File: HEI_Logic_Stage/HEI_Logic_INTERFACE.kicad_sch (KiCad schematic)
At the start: 99 parts, among them J1 Conn_02x07_Odd_Even, J2 Conn_02x07_Odd_Even, J4 430450813_Molex, U1 CD40109BQNSRQ1, U16 TLV9051IDBVR, U3 TLV9051IDBVR, U4 TLV9051IDBVR, U7 TLV9051IDBVR, U8 TLV9051IDBVR

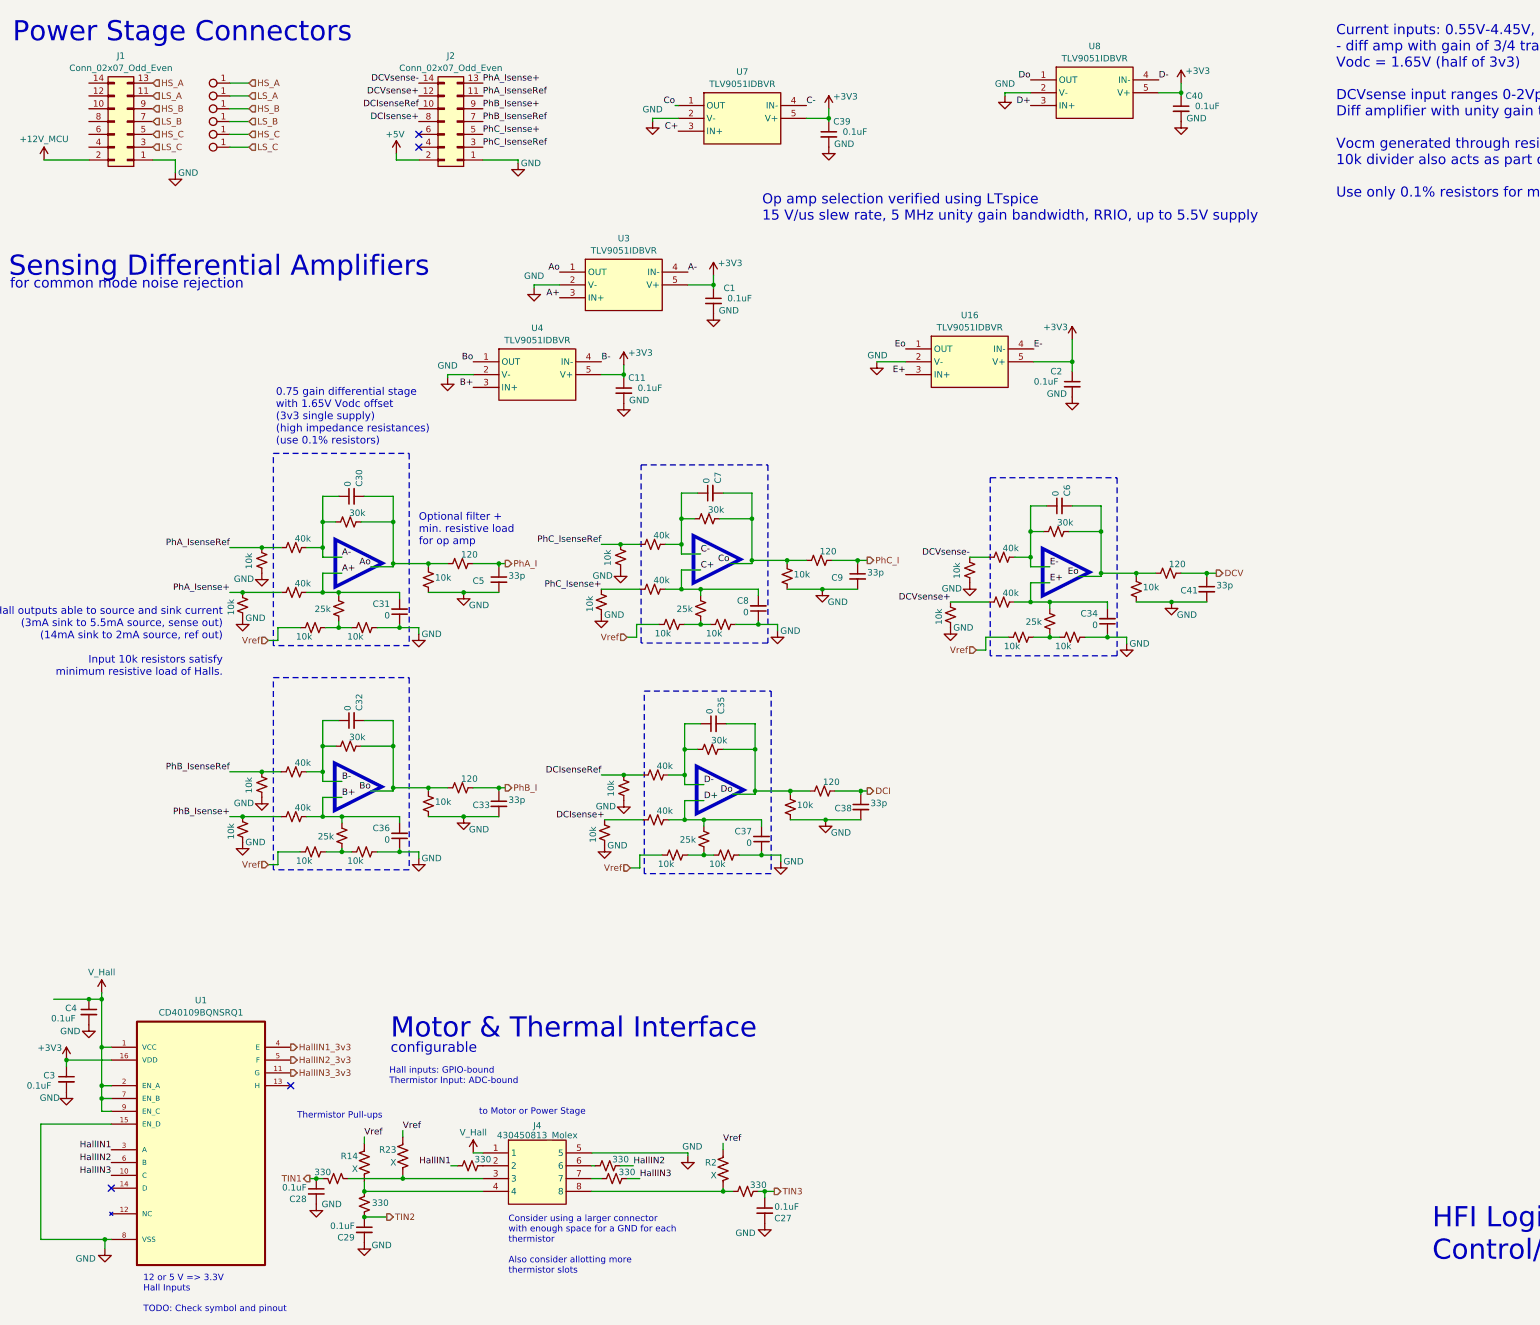
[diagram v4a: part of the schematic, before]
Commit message: almost completed new logic layout
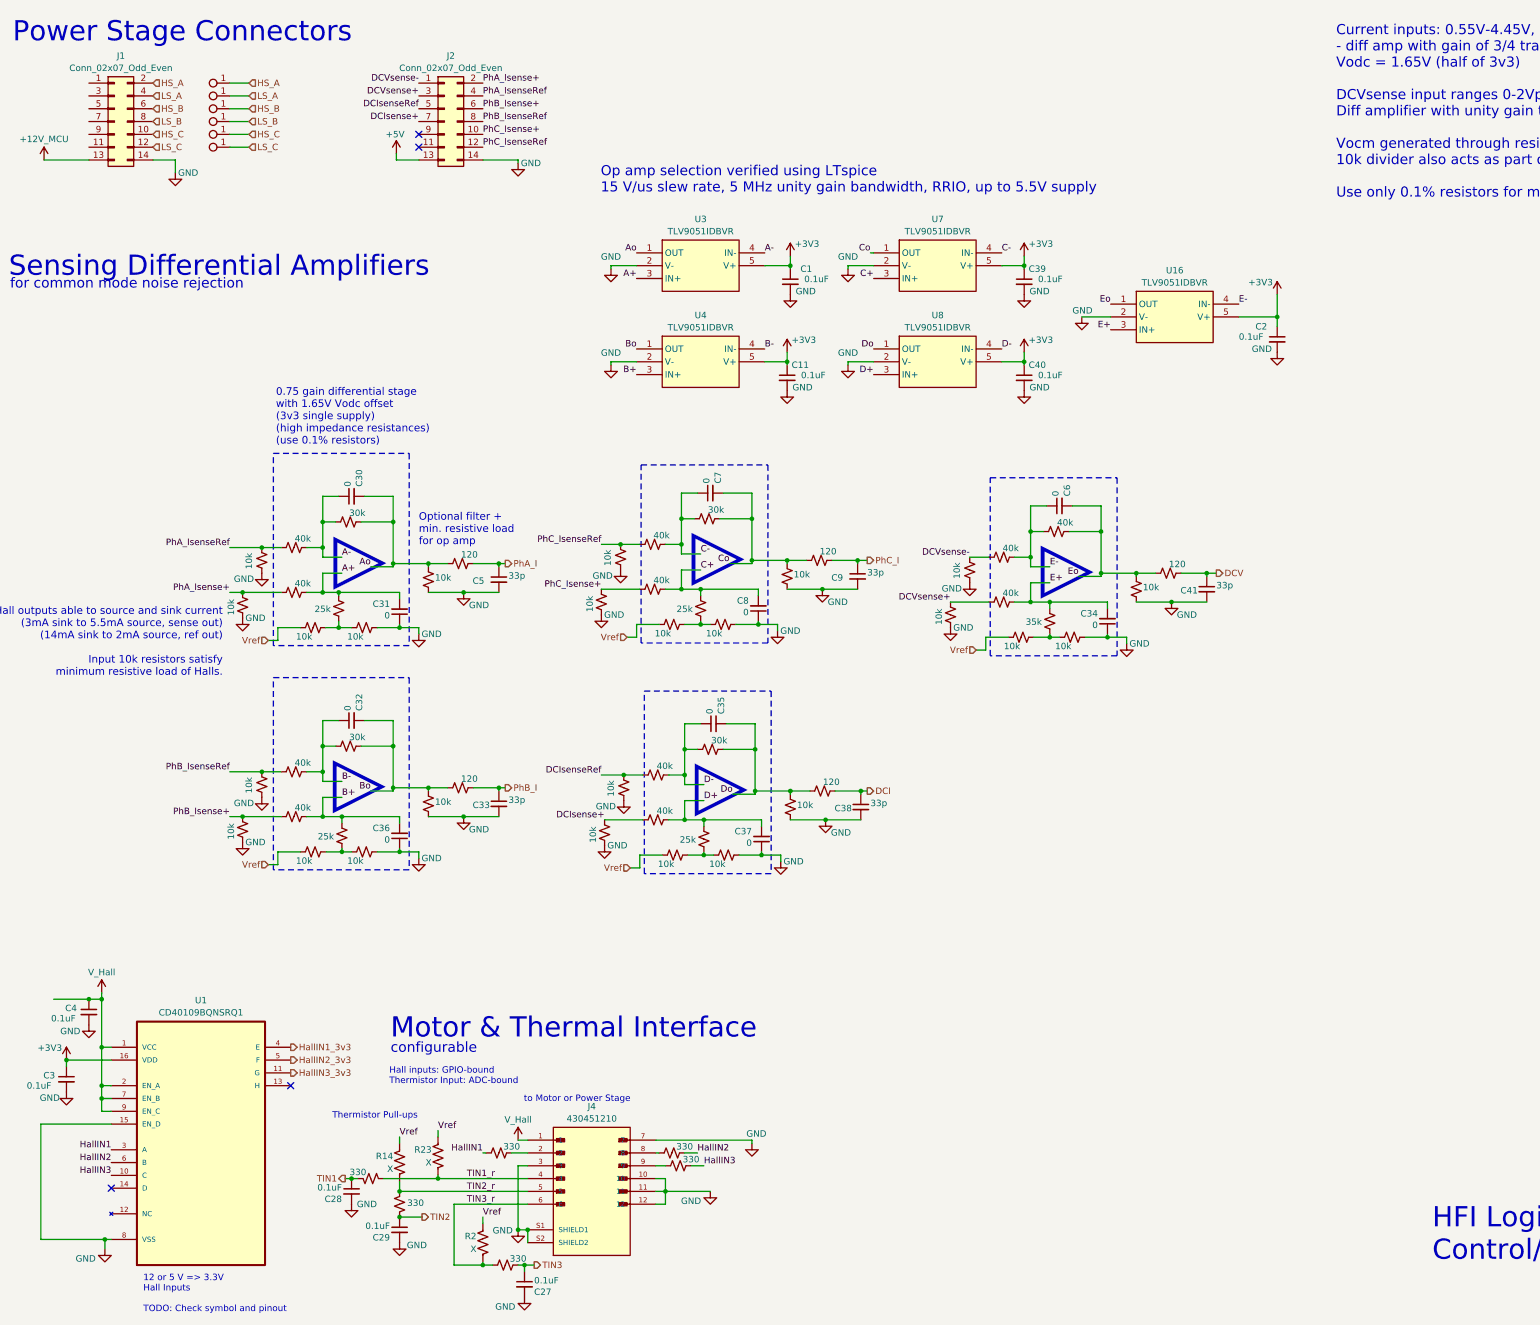
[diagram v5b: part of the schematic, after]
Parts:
- removed J4: 430450813_Molex, Connector_Molex:Molex_Micro-Fit_3.0_43045-0812_2x04_P3.00mm_Vertical, symbol GTSR_symbol_lib:2068320801_Molex
- added J4: 430451210, HEI_Logic:MOLEX_430451210, symbol HEI_Logic:430451210
- J1, J2: footprint Connector_PinHeader_2.54mm:PinHeader_2x07_P2.54mm_Horizontal -> Connector_PinHeader_2.54mm:PinHeader_2x07_P2.54mm_Vertical_SMD
- R71: value 25k -> 35k
- R72: value 30k -> 40k
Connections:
- net +12V_MCU: now also J1.13 (Pin_13); no longer J1.2 (Pin_2)
- net +5V: now also J2.13 (Pin_13); no longer J2.2 (Pin_2)
- net DCIsense+: now also J2.7 (Pin_7); no longer J2.8 (Pin_8)
- net DCIsenseRef: now also J2.5 (Pin_5); no longer J2.10 (Pin_10)
- net DCVsense+: now also J2.3 (Pin_3); no longer J2.12 (Pin_12)
- net DCVsense-: now also J2.1 (Pin_1); no longer J2.14 (Pin_14)
- net GND: now also J1.14 (Pin_14), J2.14 (Pin_14), J4.10, J4.11, J4.12, J4.3, J4.7, J4.S1 (SHIELD1), J4.S2 (SHIELD2); no longer J1.1 (Pin_1), J2.1 (Pin_1)
- net HS_A: now also J1.2 (Pin_2); no longer J1.13 (Pin_13)
- net HS_B: now also J1.6 (Pin_6); no longer J1.9 (Pin_9)
- net HS_C: now also J1.10 (Pin_10); no longer J1.5 (Pin_5)
- net LS_A: now also J1.4 (Pin_4); no longer J1.11 (Pin_11)
- net LS_B: now also J1.8 (Pin_8); no longer J1.7 (Pin_7)
- net LS_C: now also J1.12 (Pin_12); no longer J1.3 (Pin_3)
- net PhA_Isense+: now also J2.2 (Pin_2); no longer J2.13 (Pin_13)
- net PhA_IsenseRef: now also J2.4 (Pin_4); no longer J2.11 (Pin_11)
- net PhB_Isense+: now also J2.6 (Pin_6); no longer J2.9 (Pin_9)
- net PhB_IsenseRef: now also J2.8 (Pin_8); no longer J2.7 (Pin_7)
- net PhC_Isense+: now also J2.10 (Pin_10); no longer J2.5 (Pin_5)
- net PhC_IsenseRef: now also J2.12 (Pin_12); no longer J2.3 (Pin_3)
- net V_Hall: now also J4.1
- net at R15.2: now also J4.2
- net TIN2_r: now reaches R14.2, R35.1
- net TIN2_r: now also J4.5
- net TIN1_r: now reaches R23.2, R34.1
- net TIN1_r: now also J4.4
- net at R22.1: now also J4.8
- net at R24.1: now also J4.9
- net TIN3_r: now reaches R2.2, R33.1
- net TIN3_r: now also J4.6
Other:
- note removed: "Consider using a larger connector with enough space for a GND for each thermistor Also consider allotting more thermistor slots"
- moved on the sheet: C1, C11, C2, C27, C28, C29, C39, C40, J1, J2, R14, R2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

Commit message: final tweaks to logic, silkscreen not done
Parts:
- added FB1, FB2: ~, Resistor_SMD:R_0805_2012Metric, symbol Device:FerriteBead
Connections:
- net +12V_MCU: now also FB1.2; no longer J1.13 (Pin_13)
- net +5V: now also FB2.2; no longer J2.13 (Pin_13)
- net GND: now also J1.1 (Pin_1), J1.11 (Pin_11), J1.3 (Pin_3), J1.5 (Pin_5), J1.7 (Pin_7), J1.9 (Pin_9), J2.11 (Pin_11), J2.9 (Pin_9)
- new net: FB2.1, J2.13 (Pin_13)
- new net: FB1.1, J1.13 (Pin_13)
- no-connect marks 4 -> 2

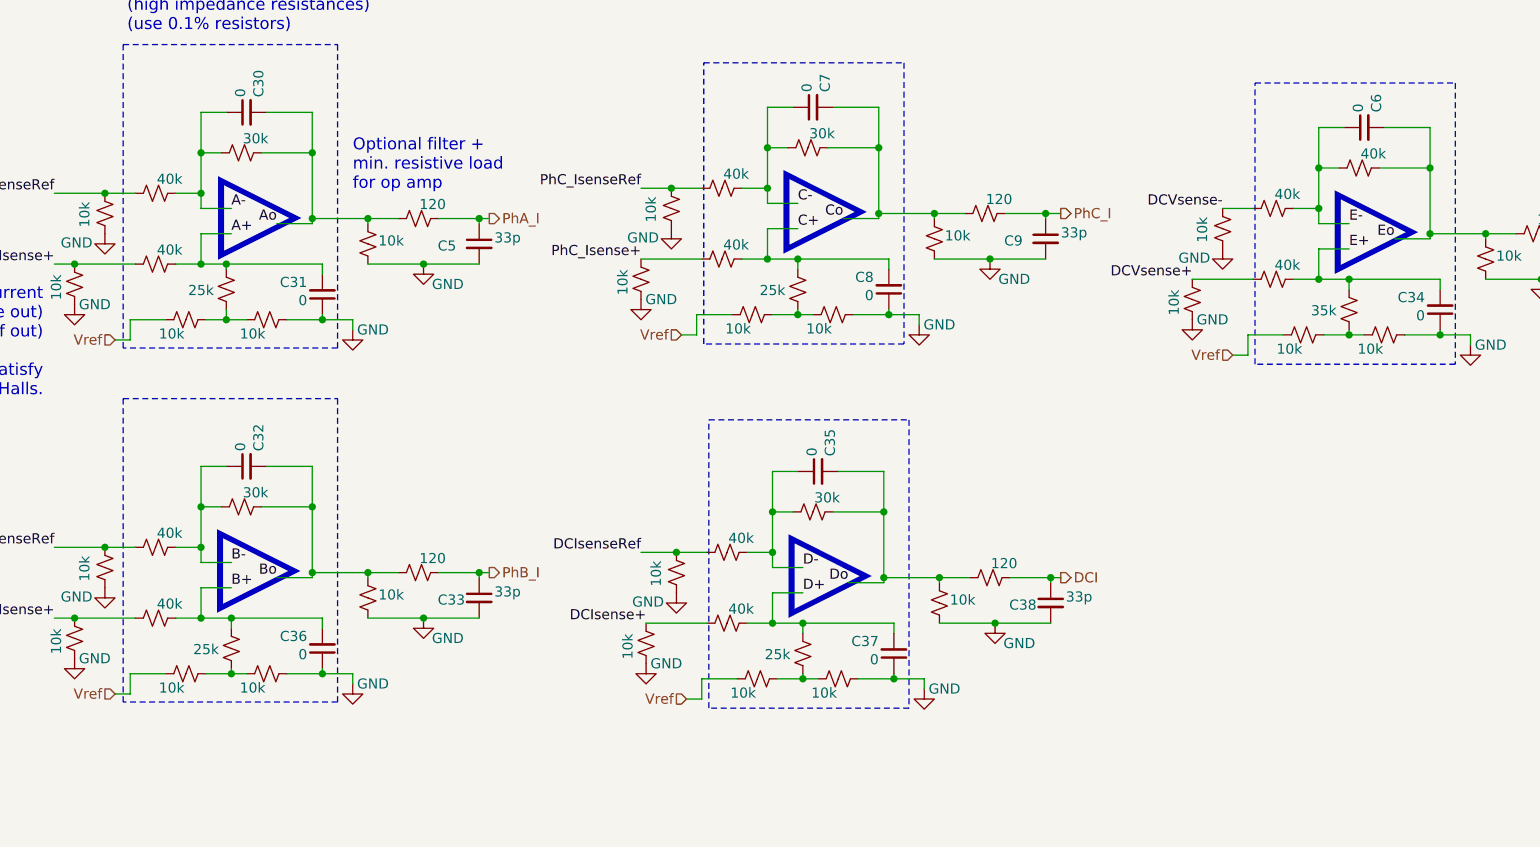
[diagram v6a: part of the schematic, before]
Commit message: updated logic diffamps with avail. resistors
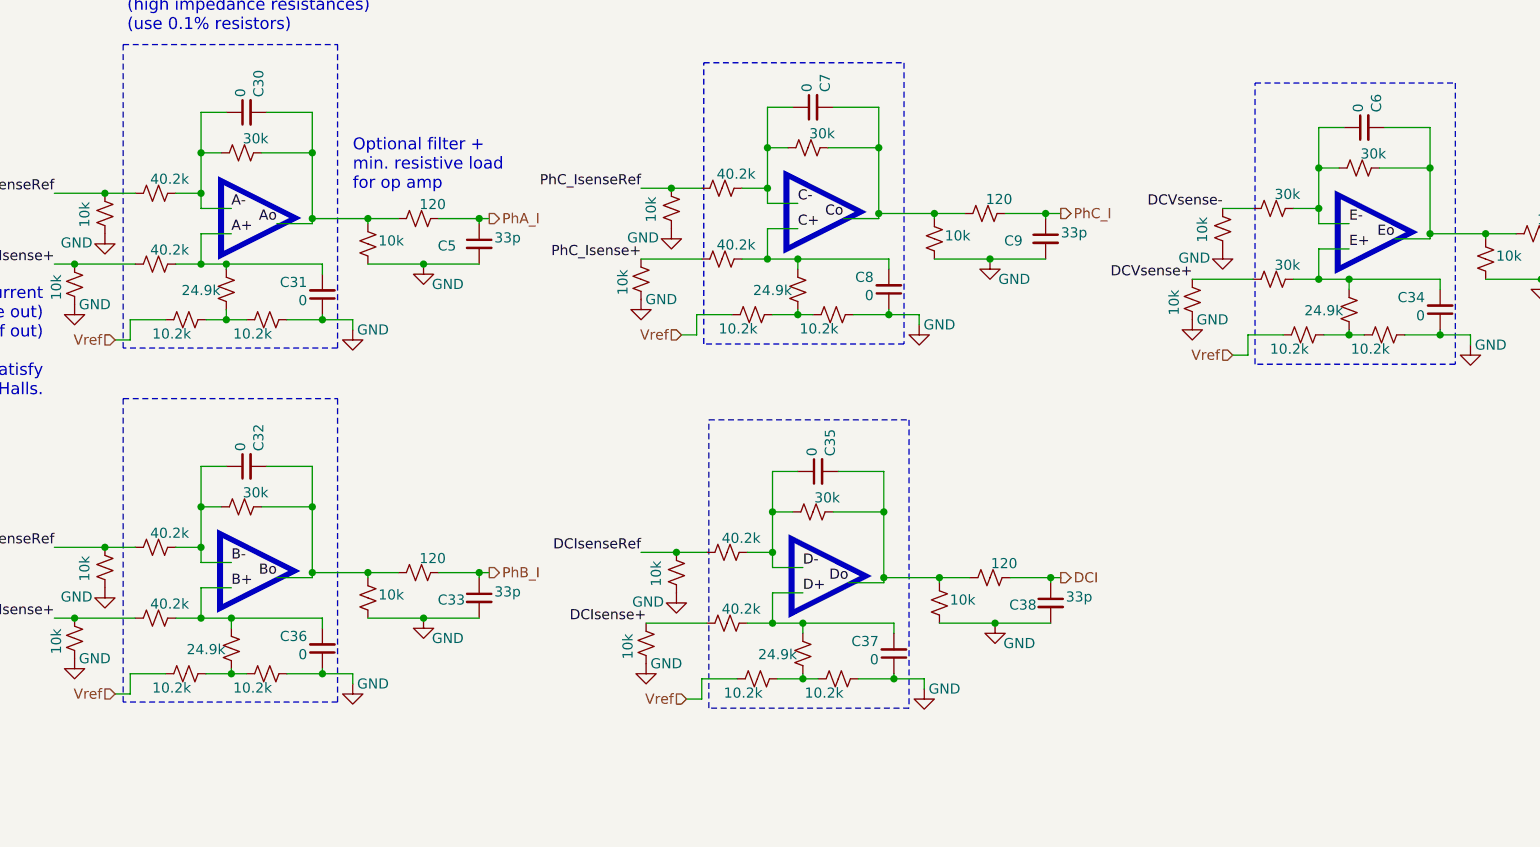
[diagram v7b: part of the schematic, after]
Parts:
- R25, R26, R46, R49, R56, R57, R59, R65, R68, R77: value 10k -> 10.2k
- R31, R32, R36, R37, R55, R58, R66, R67: value 40k -> 40.2k
- R40, R47, R53, R60: value 25k -> 24.9k
- R63, R64, R72: value 40k -> 30k
- R71: value 35k -> 24.9k
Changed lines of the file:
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@@
 			)
 		)
-		(property "Value" "40k"
+		(property "Value" "30k"
 			(at 229.743 120.777 90)
 			(effects
@@
 			)
 		)
-		(property "Value" "40k"
+		(property "Value" "40.2k"
 			(at 149.733 132.207 90)
 			(effects
@@
 			)
 		)
-		(property "Value" "10k"
+		(property "Value" "10.2k"
 			(at 89.027 143.383 90)
 			(effects
@@
 			)
 		)
-		(property "Value" "40k"
+		(property "Value" "40.2k"
 			(at 149.733 123.317 90)
 			(effects
@@
 			)
 		)
-		(property "Value" "35k"
+		(property "Value" "24.9k"
 			(at 223.52 140.462 0)
 			(effects
@@
 			)
 		)
-		(property "Value" "25k"
+		(property "Value" "24.9k"
 			(at 154.94 183.642 0)
 			(effects
@@
 			)
 		)
-		(property "Value" "10k"
+		(property "Value" "10.2k"
 			(at 160.782 188.468 90)
 			(effects
@@
 			)
 		)
-		(property "Value" "10k"
+		(property "Value" "10.2k"
 			(at 149.987 142.748 90)
 			(effects
@@
 			)
 		)
-		(property "Value" "10k"
+		(property "Value" "10.2k"
 			(at 219.202 145.288 90)
 			(effects
@@
 			)
 		)
-		(property "Value" "40k"
+		(property "Value" "40.2k"
 			(at 150.368 169.037 90)
 			(effects
@@
 			)
 		)
-		(property "Value" "10k"
+		(property "Value" "10.2k"
 			(at 89.027 187.833 90)
 			(effects
@@
 			)
 		)
-		(property "Value" "40k"
+		(property "Value" "40.2k"
 			(at 150.368 177.927 90)
 			(effects
@@
 			)
 		)
-		(property "Value" "40k"
+		(property "Value" "40.2k"
 			(at 78.613 132.842 90)
 			(effects
@@
 			)
 		)
-		(property "Value" "10k"
+		(property "Value" "10.2k"
 			(at 78.867 143.383 90)
 			(effects
@@
 			)
 		)
-		(property "Value" "25k"
+		(property "Value" "24.9k"
 			(at 154.305 137.922 0)
 			(effects
@@
 			)
 		)
-		(property "Value" "25k"
+		(property "Value" "24.9k"
 			(at 83.185 183.007 0)
 			(effects
@@
 			)
 		)
-		(property "Value" "10k"
+		(property "Value" "10.2k"
 			(at 160.147 142.748 90)
 			(effects
@@
 			)
 		)
-		(property "Value" "10k"
+		(property "Value" "10.2k"
 			(at 229.362 145.288 90)
 			(effects
@@
 			)
 		)
-		(property "Value" "40k"
+		(property "Value" "30k"
 			(at 218.948 134.747 90)
 			(effects
@@
 			)
 		)
-		(property "Value" "40k"
+		(property "Value" "40.2k"
 			(at 78.613 177.292 90)
 			(effects
@@
 			)
 		)
-		(property "Value" "10k"
+		(property "Value" "10.2k"
 			(at 150.622 188.468 90)
 			(effects
@@
 			)
 		)
-		(property "Value" "25k"
+		(property "Value" "24.9k"
 			(at 82.55 137.922 0)
 			(effects
@@
 			)
 		)
-		(property "Value" "10k"
+		(property "Value" "10.2k"
 			(at 78.867 187.833 90)
 			(effects
@@
 			)
 		)
-		(property "Value" "40k"
+		(property "Value" "40.2k"
 			(at 78.613 168.402 90)
 			(effects
@@
 			)
 		)
-		(property "Value" "40k"
+		(property "Value" "30k"
 			(at 218.948 125.857 90)
 			(effects
@@
 			)
 		)
-		(property "Value" "40k"
+		(property "Value" "40.2k"
 			(at 78.613 123.952 90)
 			(effects

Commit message: schematic updates - logic
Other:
- note removed: "12 or 5 V => 3.3V Hall Inputs TODO: Check symbol and pinout"
- note removed: "Thermistor Pull-ups"
- moved on the sheet: C1, C11, C2, C27, C28, C29, C3, C30, C31, C32, C33, C34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
